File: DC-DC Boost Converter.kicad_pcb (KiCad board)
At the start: 2 copper layers, 13 parts, among them J1 Conn_01x01_Pin, J2 Conn_01x01_Pin, J3 Conn_01x01_Pin, J4 Conn_01x01_Pin

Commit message: Placed Footprints in PCB Editor
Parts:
- moved J4 122.1 mm to (180.2, 26.8)
- moved C4 120.1 mm to (173.5, 38.0)
- moved L1 120.0 mm to (163.1, 31.5)
- moved J3 118.9 mm to (180.2, 44.8)
- moved C3 108.4 mm to (173.6, 29.8)
- moved RV1 105.5 mm to (167.0, 42.8)
- moved VR1 101.4 mm to (147.0, 33.0), turned to 90 degrees
- moved R1 90.4 mm to (155.0, 43.8)
- moved D1 89.7 mm to (147.5, 44.2), turned to 180 degrees
- moved C1 84.0 mm to (138.0, 40.0), turned to 90 degrees
- moved C2 72.1 mm to (138.0, 44.8)
- moved J1 70.5 mm to (130.5, 26.8)
- moved J2 69.0 mm to (130.5, 44.8)

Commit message: Placed Footprints at their Position
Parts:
- moved C1 64.0 mm to (135.5, 104.0)
- moved C2 64.0 mm to (135.5, 108.8)
- moved C3 64.0 mm to (171.1, 93.8)
- moved C4 64.0 mm to (171.0, 102.0)
- moved D1 64.0 mm to (145.0, 108.2)
- moved J1 64.0 mm to (128.0, 90.8)
- moved J2 64.0 mm to (128.0, 108.8)
- moved J3 64.0 mm to (177.8, 108.8)
- moved J4 64.0 mm to (177.8, 90.8)
- moved L1 64.0 mm to (160.6, 95.5)
- moved R1 64.0 mm to (152.5, 107.8)
- moved RV1 64.0 mm to (164.5, 106.8)
- moved VR1 64.0 mm to (144.5, 97.0)
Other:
- board outline added: 54.8 x 23.2 mm
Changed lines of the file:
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@@
 	(footprint "Resistor_SMD:R_1206_3216Metric"
 		(layer "F.Cu")
-		(at 155.0375 43.75)
+		(at 152.5375 107.75)
 		(descr "Resistor SMD 1206 (3216 Metric), square (rectangular) end terminal, IPC-7351 nominal, (Body size source: IPC-SM-782 page 72, https://www.pcb-3d.com/wordpress/wp-content/uploads/ipc-sm-782a_amendment_1_and_2.pdf), generated with kicad-footprint-generator")
 		(tags "resistor")
@@
 	(footprint "Diode_SMD:D_SMA"
 		(layer "F.Cu")
-		(at 147.5 44.25 180)
+		(at 145 108.25 180)
 		(descr "Diode SMA (DO-214AC)")
 		(tags "Diode SMA (DO-214AC)")
@@
 	(footprint "Connector_PinHeader_2.54mm:PinHeader_1x01_P2.54mm_Vertical"
 		(layer "F.Cu")
-		(at 130.5 26.75)
+		(at 128 90.75)
 		(descr "Through hole straight pin header, 1x01, 2.54mm pitch, single row")
 		(tags "Through hole pin header THT 1x01 2.54mm single row")
 		(property "Reference" "J1"
-			(at 0 -2.38 0)
+			(at 2.75 -0.25 0)
 			(layer "F.SilkS")
 			(effects
@@
 	(footprint "Capacitor_THT:C_Radial_D6.3mm_H11.0mm_P2.50mm"
 		(layer "F.Cu")
-		(at 173.5 38)
+		(at 171 102)
 		(descr "C, Radial series, Radial, pin pitch=2.50mm, diameter=6.3mm, height=11mm, Non-Polar Electrolytic Capacitor")
 		(tags "C Radial series Radial pin pitch 2.50mm diameter 6.3mm height 11mm Non-Polar Electrolytic Capacitor")
@@
 	(footprint "Connector_PinHeader_2.54mm:PinHeader_1x01_P2.54mm_Vertical"
 		(layer "F.Cu")
-		(at 180.25 44.75)
+		(at 177.75 108.75)
 		(descr "Through hole straight pin header, 1x01, 2.54mm pitch, single row")
 		(tags "Through hole pin header THT 1x01 2.54mm single row")
 		(property "Reference" "J3"
-			(at 0 -2.38 0)
+			(at -2.75 0.25 0)
 			(layer "F.SilkS")
 			(effects
@@
 	(footprint "Capacitor_THT:C_Radial_D6.3mm_H11.0mm_P2.50mm"
 		(layer "F.Cu")
-		(at 138 40 90)
+		(at 135.5 104 90)
 		(descr "C, Radial series, Radial, pin pitch=2.50mm, diameter=6.3mm, height=11mm, Non-Polar Electrolytic Capacitor")
 		(tags "C Radial series Radial pin pitch 2.50mm diameter 6.3mm height 11mm Non-Polar Electrolytic Capacitor")
@@
 	(footprint "Connector_PinHeader_2.54mm:PinHeader_1x01_P2.54mm_Vertical"
 		(layer "F.Cu")
-		(at 180.25 26.75)
+		(at 177.75 90.75)
 		(descr "Through hole straight pin header, 1x01, 2.54mm pitch, single row")
 		(tags "Through hole pin header THT 1x01 2.54mm single row")
 		(property "Reference" "J4"
-			(at 0 -2.38 0)
+			(at -2.75 0 0)
 			(layer "F.SilkS")
 			(effects
@@
 	(footprint "Footprints:DPAK170P1435X465-6N"
 		(layer "F.Cu")
-		(at 147 33 90)
+		(at 144.5 97 90)
 		(property "Reference" "VR1"
 			(at 0.25 -6.75 90)
@@
 	(footprint "Capacitor_SMD:C_0805_2012Metric"
 		(layer "F.Cu")
-		(at 173.55 29.75)
+		(at 171.05 93.75)
 		(descr "Capacitor SMD 0805 (2012 Metric), square (rectangular) end terminal, IPC-7351 nominal, (Body size source: IPC-SM-782 page 76, https://www.pcb-3d.com/wordpress/wp-content/uploads/ipc-sm-782a_amendment_1_and_2.pdf, https://docs.google.com/spreadsheets/d/1BsfQQcO9C6DZCsRaXUlFlo91Tg2WpOkGARC1WS5S8t0/edit?usp=sharing), generated with kicad-footprint-generator")
 		(tags "capacitor")
@@
 	(footprint "Inductor_SMD:L_12x12mm_H8mm"
 		(layer "F.Cu")
-		(at 163.05 31.5)
+		(at 160.55 95.5)
 		(descr "Choke, SMD, 12x12mm 8mm height")
 		(tags "Choke SMD")
@@
 	(footprint "Connector_PinHeader_2.54mm:PinHeader_1x01_P2.54mm_Vertical"
 		(layer "F.Cu")
-		(at 130.5 44.75)
+		(at 128 108.75)
 		(descr "Through hole straight pin header, 1x01, 2.54mm pitch, single row")
 		(tags "Through hole pin header THT 1x01 2.54mm single row")
 		(property "Reference" "J2"
-			(at 0 -2.38 0)
+			(at 2.75 -0.25 0)
 			(layer "F.SilkS")
 			(effects
@@
 	(footprint "Capacitor_SMD:C_0805_2012Metric"
 		(layer "F.Cu")
-		(at 138 44.75)
+		(at 135.5 108.75)
 		(descr "Capacitor SMD 0805 (2012 Metric), square (rectangular) end terminal, IPC-7351 nominal, (Body size source: IPC-SM-782 page 76, https://www.pcb-3d.com/wordpress/wp-content/uploads/ipc-sm-782a_amendment_1_and_2.pdf, https://docs.google.com/spreadsheets/d/1BsfQQcO9C6DZCsRaXUlFlo91Tg2WpOkGARC1WS5S8t0/edit?usp=sharing), generated with kicad-footprint-generator")
 		(tags "capacitor")
@@
 	(footprint "Potentiometer_THT:Potentiometer_Bourns_3296W_Vertical"
 		(layer "F.Cu")
-		(at 167 42.75)
+		(at 164.5 106.75)
 		(descr "Potentiometer, vertical, Bourns 3296W, https://www.bourns.com/pdfs/3296.pdf")
 		(tags "Potentiometer vertical Bourns 3296W")
@@
 		)
 	)
+	(gr_rect
+		(start 125.5 88)
+		(end 180.25 111.25)
+		(stroke
+			(width 0.05)
+			(type default)
+		)
+		(fill no)
+		(layer "Edge.Cuts")
+	)
 	(embedded_fonts no)

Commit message: Added tracks to PCB Editor
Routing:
- net GND: track 0.00 -> 85.8 mm, vias 0 -> 1
- net Net-(J1-Pin_1): track 0.00 -> 51.6 mm
- net Net-(D1-K): track 0.00 -> 49.5 mm
- net Net-(D1-A): track 0.00 -> 38.1 mm
- net Net-(VR1-FB): track 0.00 -> 21.6 mm

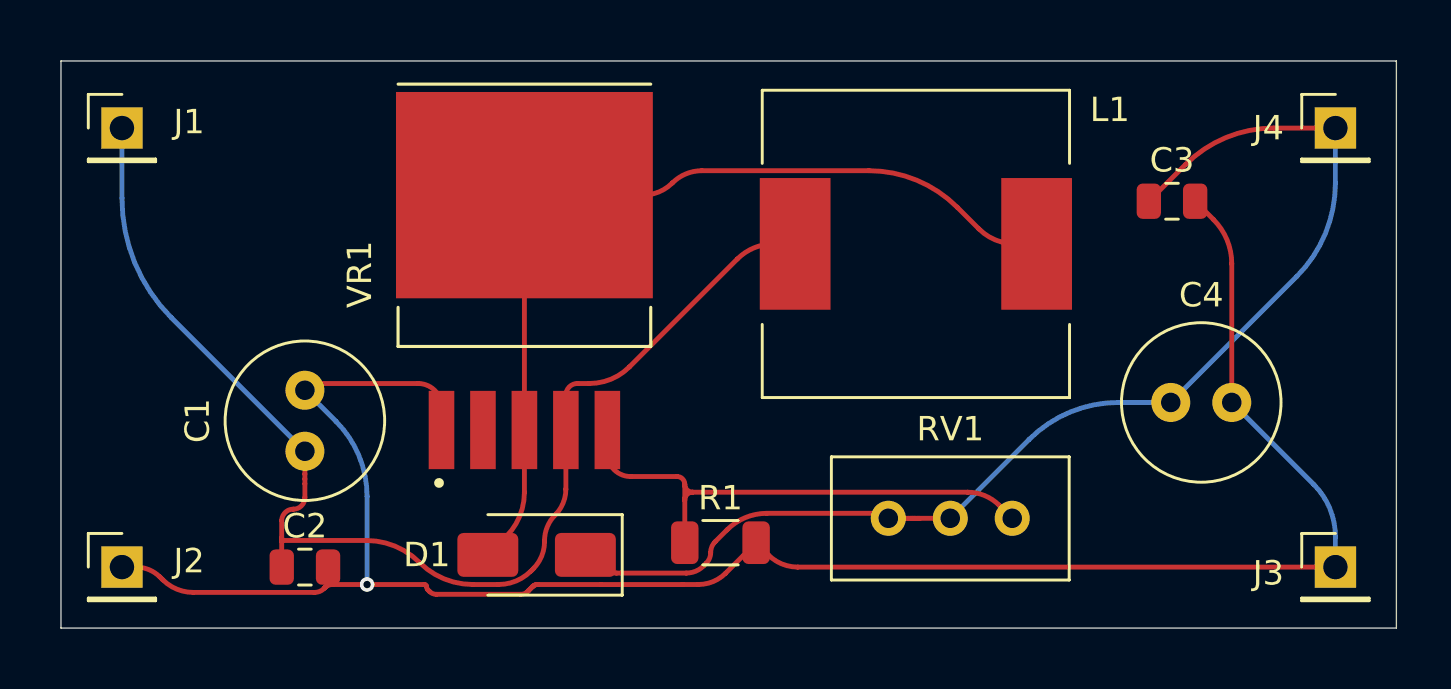
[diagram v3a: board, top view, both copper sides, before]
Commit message: Extracted 3D model and Built Complete PCB
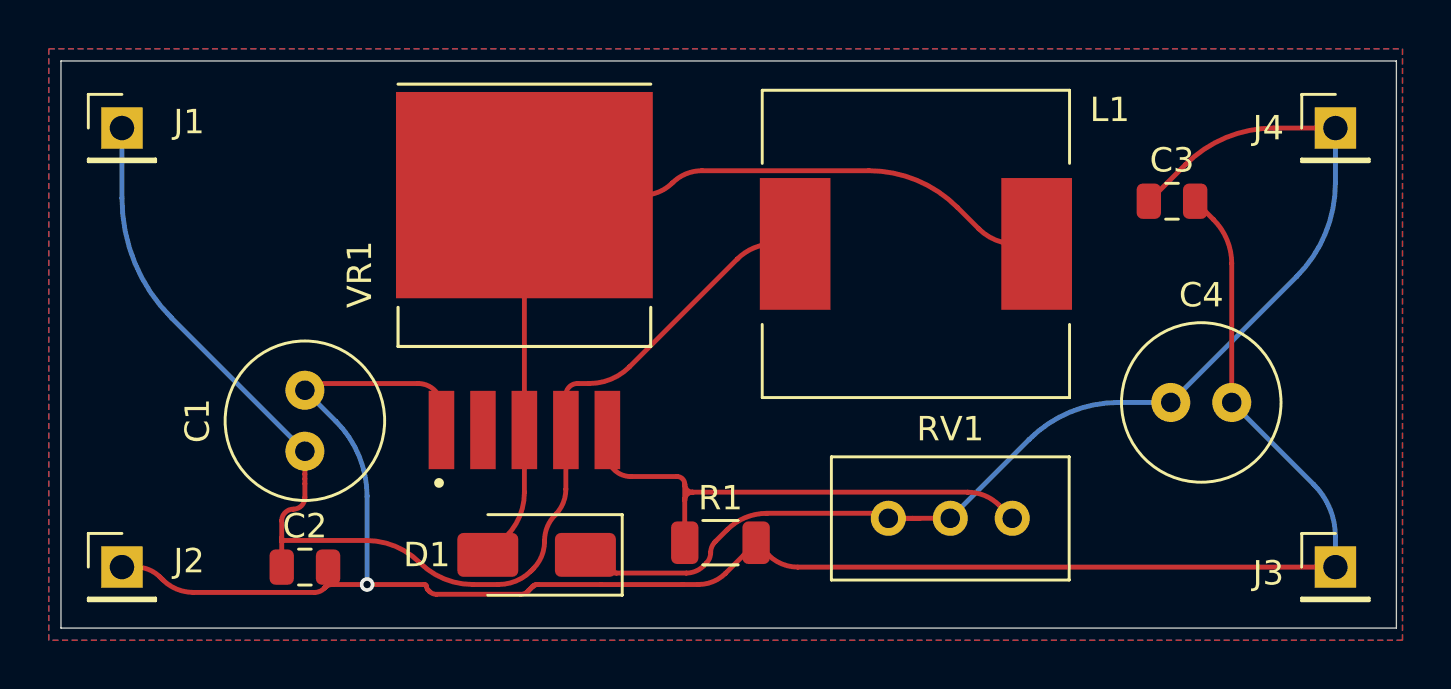
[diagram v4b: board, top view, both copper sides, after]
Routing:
- added copper zone on B.Cu, net GND
- added copper zone on F.Cu, net GND
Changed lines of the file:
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@@
 		)
 		(embedded_fonts no)
-		(model "${KICAD9_3DMODEL_DIR}/Resistor_SMD.3dshapes/R_1206_3216Metric.step"
+		(model "C:/Users/91755/AppData/Local/Programs/KiCad/9.0/share/kicad/3dmodels/Resistor_SMD.3dshapes/R_1206_3216Metric.step"
 			(offset
 				(xyz 0 0 0)
@@
 		)
 		(embedded_fonts no)
-		(model "${KICAD9_3DMODEL_DIR}/Diode_SMD.3dshapes/D_SMA.step"
+		(model "C:/Users/91755/AppData/Local/Programs/KiCad/9.0/share/kicad/3dmodels/Diode_SMD.3dshapes/D_SMA.step"
 			(offset
 				(xyz 0 0 0)
@@
 		)
 		(embedded_fonts no)
-		(model "${KICAD9_3DMODEL_DIR}/Connector_PinHeader_2.54mm.3dshapes/PinHeader_1x01_P2.54mm_Vertical.step"
+		(model "C:/Users/91755/AppData/Local/Programs/KiCad/9.0/share/kicad/3dmodels/Connector_PinHeader_2.54mm.3dshapes/PinHeader_1x01_P2.54mm_Vertical.step"
 			(offset
 				(xyz 0 0 0)
@@
 		)
 		(embedded_fonts no)
-		(model "${KICAD9_3DMODEL_DIR}/Capacitor_THT.3dshapes/C_Radial_D6.3mm_H11.0mm_P2.50mm.step"
+		(model "${KICAD9_3DMODEL_DIR}/C_Radial_D6.3mm_H11.0mm_P2.50mm.step"
 			(offset
 				(xyz 0 0 0)
@@
 		)
 		(embedded_fonts no)
-		(model "${KICAD9_3DMODEL_DIR}/Connector_PinHeader_2.54mm.3dshapes/PinHeader_1x01_P2.54mm_Vertical.step"
+		(model "C:/Users/91755/AppData/Local/Programs/KiCad/9.0/share/kicad/3dmodels/Connector_PinHeader_2.54mm.3dshapes/PinHeader_1x01_P2.54mm_Vertical.step"
 			(offset
 				(xyz 0 0 0)
@@
 		)
 		(embedded_fonts no)
-		(model "${KICAD9_3DMODEL_DIR}/Capacitor_THT.3dshapes/C_Radial_D6.3mm_H11.0mm_P2.50mm.step"
+		(model "${KICAD9_3DMODEL_DIR}/C_Radial_D6.3mm_H11.0mm_P2.50mm.step"
 			(offset
 				(xyz 0 0 0)
@@
 		)
 		(embedded_fonts no)
-		(model "${KICAD9_3DMODEL_DIR}/Connector_PinHeader_2.54mm.3dshapes/PinHeader_1x01_P2.54mm_Vertical.step"
+		(model "C:/Users/91755/AppData/Local/Programs/KiCad/9.0/share/kicad/3dmodels/Connector_PinHeader_2.54mm.3dshapes/PinHeader_1x01_P2.54mm_Vertical.step"
 			(offset
 				(xyz 0 0 0)
@@
 		)
 		(embedded_fonts no)
+		(model "${KIPRJMOD}/Libraries/3D Models/XL6009.step"
+			(offset
+				(xyz 0 0 0)
+			)
+			(scale
+				(xyz 1 1 1)
+			)
+			(rotate
+				(xyz -90 -0 -0)
+			)
+		)
 	)
 	(footprint "Capacitor_SMD:C_0805_2012Metric"
@@
 		)
 		(embedded_fonts no)
-		(model "${KICAD9_3DMODEL_DIR}/Capacitor_SMD.3dshapes/C_0805_2012Metric.step"
+		(model "C:/Users/91755/AppData/Local/Programs/KiCad/9.0/share/kicad/3dmodels/Capacitor_SMD.3dshapes/C_0805_2012Metric.step"
 			(offset
 				(xyz 0 0 0)
@@
 		)
 		(embedded_fonts no)
-		(model "${KICAD9_3DMODEL_DIR}/Inductor_SMD.3dshapes/L_12x12mm_H8mm.step"
+		(model "${KIPRJMOD}/Libraries/3D Models/L_12x12mm_H8mm.step"
 			(offset
 				(xyz 0 0 0)
@@
 			)
 			(rotate
-				(xyz 0 0 0)
+				(xyz -0 -0 -0)
 			)
 		)
@@
 		)
 		(embedded_fonts no)
-		(model "${KICAD9_3DMODEL_DIR}/Connector_PinHeader_2.54mm.3dshapes/PinHeader_1x01_P2.54mm_Vertical.step"
+		(model "C:/Users/91755/AppData/Local/Programs/KiCad/9.0/share/kicad/3dmodels/Connector_PinHeader_2.54mm.3dshapes/PinHeader_1x01_P2.54mm_Vertical.step"
 			(offset
 				(xyz 0 0 0)
@@
 		)
 		(embedded_fonts no)
-		(model "${KICAD9_3DMODEL_DIR}/Capacitor_SMD.3dshapes/C_0805_2012Metric.step"
+		(model "C:/Users/91755/AppData/Local/Programs/KiCad/9.0/share/kicad/3dmodels/Capacitor_SMD.3dshapes/C_0805_2012Metric.step"
 			(offset
 				(xyz 0 0 0)
@@
 		)
 		(embedded_fonts no)
-		(model "${KICAD9_3DMODEL_DIR}/Potentiometer_THT.3dshapes/Potentiometer_Bourns_3296W_Vertical.step"
+		(model "C:/Users/91755/AppData/Local/Programs/KiCad/9.0/share/kicad/3dmodels/Potentiometer_THT.3dshapes/Potentiometer_Bourns_3296W_Vertical.step"
 			(offset
 				(xyz 0 0 0)
@@
 		(net 5)
 	)
+	(zone
+		(net 2)
+		(net_name "GND")
+		(layers "F.Cu" "B.Cu")
+		(hatch edge 0.5)
+		(connect_pads
+			(clearance 0.5)
+		)
+		(min_thickness 0.25)
+		(filled_areas_thickness no)
+		(fill yes
+			(thermal_gap 0.5)
+			(thermal_bridge_width 0.5)
+		)
+		(polygon
+			(pts
+				(xy 125 87.5) (xy 180.5 87.5) (xy 180.5 111.75) (xy 125 111.75)
+			)
+		)
+	)
 	(embedded_fonts no)
